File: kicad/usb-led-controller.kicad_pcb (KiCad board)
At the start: 4 copper layers, 70 x 30 mm, 99 parts, among them J1 SWD, J2 PWR, J3 USB, J4 PWM_0, J5 PWM_1, J6 WS2812_0, J7 WS2812_1, Q1 NVS4409N, Q2 NVS4409N, Q3 NVS4409N, Q4 NVS4409N, Q5 NVS4409N, Q6 NVS4409N, U1 SN74LV1T125, U2 SN74LV1T125, U3 EFM32HG308F64G-C-QFN24, U5 USBLC6

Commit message: Upgrading to Kicad 6
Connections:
- net /WS2812_0_~OE renamed /WS2812_0_~{OE}
- net /WS2812_1_~OE renamed /WS2812_1_~{OE}
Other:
- net class Default removed
- net class Power removed
- net class USB removed

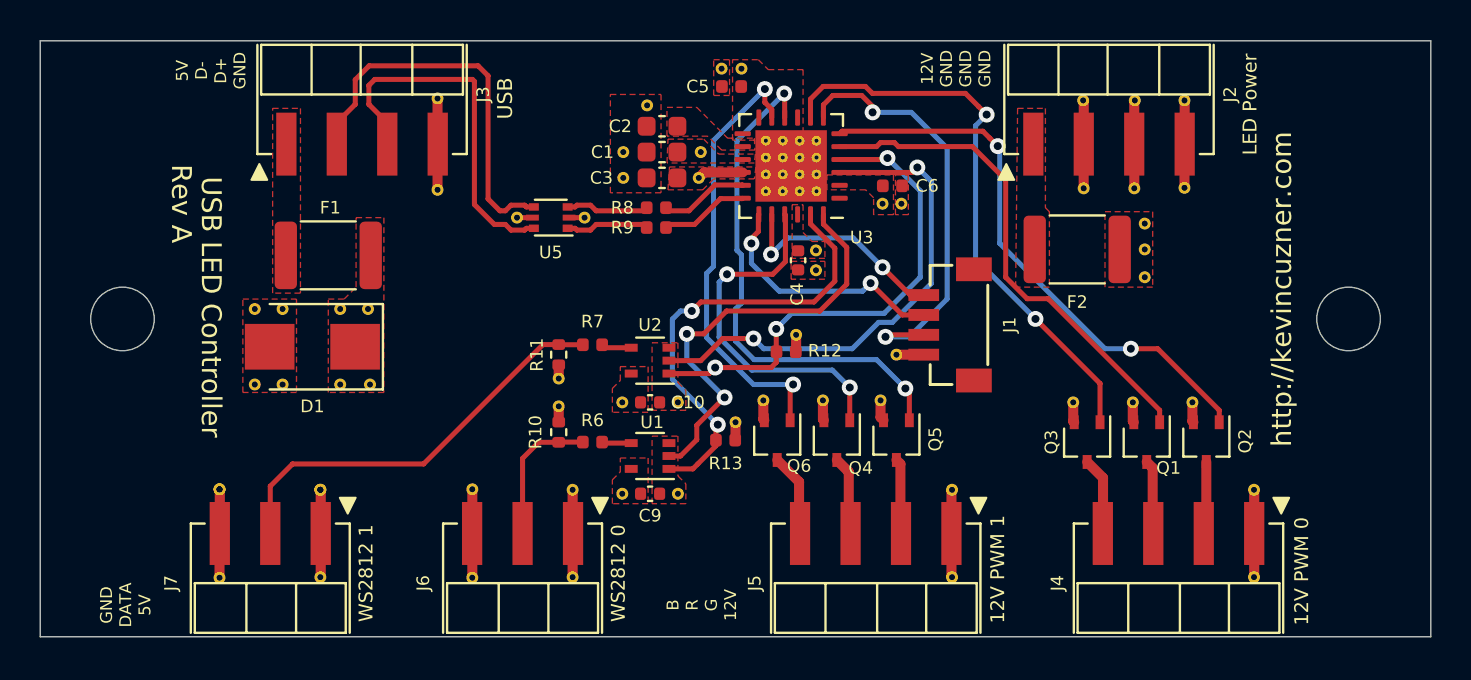
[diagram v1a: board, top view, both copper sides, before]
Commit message: Changing microcontroller to ATSAMD21E15B
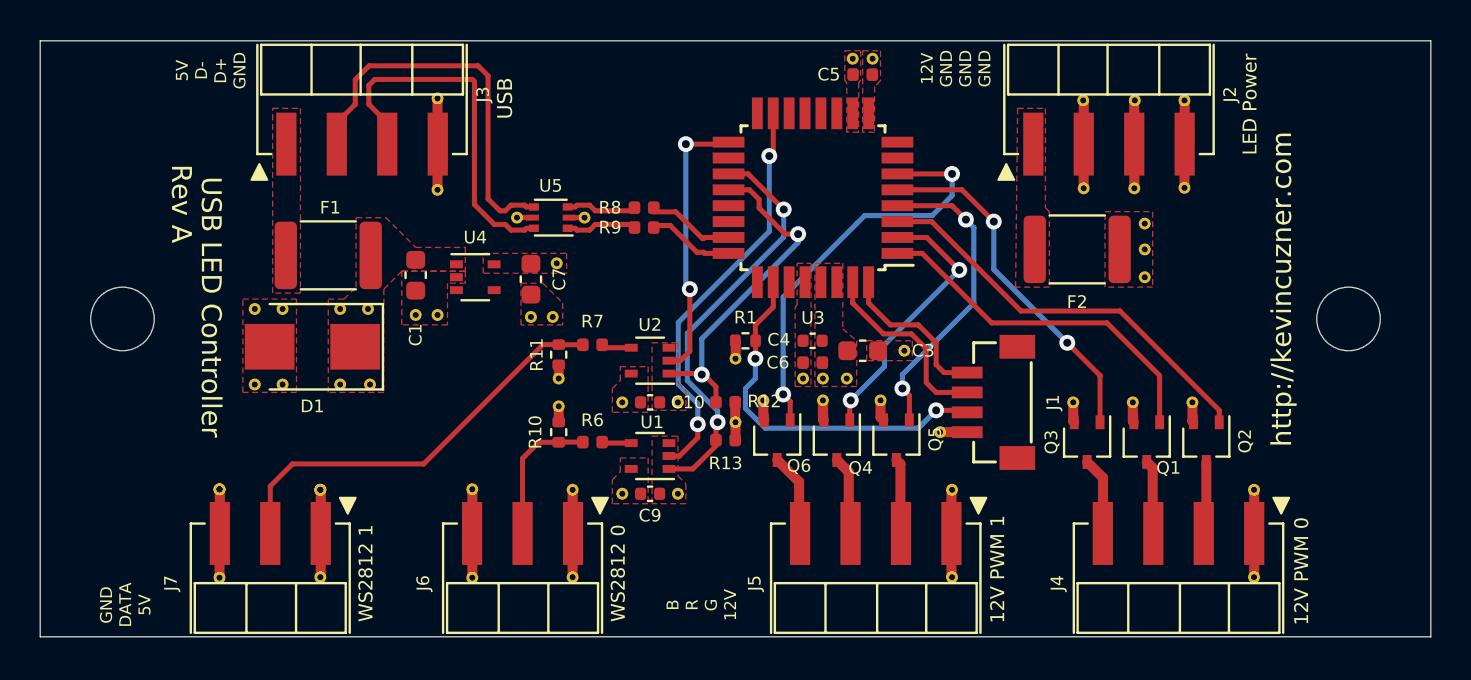
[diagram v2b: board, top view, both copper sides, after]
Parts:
- removed C2: 1u, Capacitor_SMD:C_0603_1608Metric
- removed the REF** at (163.2, 105.6)
- removed the REF** at (165.3, 101.4)
- added C7: 4u7, Capacitor_SMD:C_0603_1608Metric, F.Cu at (154.7, 112.0)
- added R1: 10K, Resistor_SMD:R_0402_1005Metric, F.Cu at (165.5, 115.1)
- added REF**: VIA-0.3_0.6-TENT, usb-led-controller:VIA-0.3_0.6-TENT, F.Cu at (175.3, 119.7)
- added REF**: VIA-0.3_0.6-TENT, usb-led-controller:VIA-0.3_0.6-TENT, F.Cu at (165.0, 116.0)
- added U4: MIC5365-3.3YC5, Package_TO_SOT_SMD:SOT-353_SC-70-5, F.Cu at (151.9, 111.9)
- U3: value EFM32HG308F64G-C-QFN24 -> ATSAMD21E15B-A; footprint Package_DFN_QFN:QFN-24-1EP_5x5mm_P0.65mm_EP3.6x3.6mm_ThermalVias -> Package_QFP:TQFP-32_7x7mm_P0.8mm
- moved REF** 18.5 mm to (155.8, 113.9)
- moved C1 13.9 mm to (148.9, 111.8), turned to -90 degrees
- moved C3 13.3 mm to (171.4, 115.6), turned to 0 degrees
- moved REF** 13.3 mm to (148.9, 113.8)
- moved REF** 12.2 mm to (154.7, 113.9)
- moved REF** 11.6 mm to (150.0, 113.8)
- moved C6 9.76 mm to (168.9, 116.2), turned to 180 degrees
- moved REF** 8.34 mm to (156.0, 111.2)
- moved REF** 7.32 mm to (171.9, 100.9)
- moved C5 6.63 mm to (171.4, 101.7)
- moved REF** 6.62 mm to (170.9, 100.9)
- moved REF** 6.46 mm to (169.4, 117.0)
- moved REF** 5.49 mm to (168.4, 117.0)
- moved J1 4.47 mm to (180.1, 118.2)
- moved C4 4.12 mm to (168.9, 115.1), turned to 180 degrees
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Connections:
- U3 pad 1: Net-(U3-Pad1) -> /GATE_0_R
- U3 pad 10: /GATE_1_G -> GND
- U3 pad 11: /GATE_1_B -> unconnected-(U3-Pad11)
- U3 pad 12: +3V3 -> unconnected-(U3-Pad12)
- U3 pad 13: +3V3 -> unconnected-(U3-Pad13)
- U3 pad 14: /UC_DECOUPLE -> unconnected-(U3-Pad14)
- U3 pad 15: +5V -> /WS2812_0_DATA_UC
- U3 pad 16: +3V3 -> unconnected-(U3-Pad16)
- U3 pad 17: /USB_D_R- -> /WS2812_1_DATA_UC
- U3 pad 18: /USB_D_R+ -> unconnected-(U3-Pad18)
- U3 pad 19: /SWCLK -> /WS2812_0_~{OE}
- U3 pad 2: +3V3 -> /GATE_1_R
- U3 pad 20: /SWDIO -> /WS2812_1_~{OE}
- U3 pad 21: /GATE_1_R -> unconnected-(U3-Pad21)
- U3 pad 22: +3V3 -> unconnected-(U3-Pad22)
- U3 pad 23: /WS2812_0_~{OE} -> /USB_D_R-
- U3 pad 24: /WS2812_0_DATA_UC -> /USB_D_R+
- U3 pad 25: GND -> unconnected-(U3-Pad25)
- U3 pad 3: /WS2812_1_DATA_UC -> /GATE_0_G
- U3 pad 4: /WS2812_1_~{OE} -> /GATE_1_G
- U3 pad 5: /GATE_0_R -> /GATE_0_B
- U3 pad 6: /GATE_0_G -> /GATE_1_B
- U3 pad 7: /NRST -> unconnected-(U3-Pad7)
- U3 pad 8: /GATE_0_B -> unconnected-(U3-Pad8)
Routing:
- net /WS2812_1_DATA_UC: track 25.4 -> 13.9 mm
- net /GATE_0_B: track 29.0 -> 17.8 mm
- net /GATE_1_G: track 26.1 -> 15.6 mm
- net /GATE_0_G: track 28.4 -> 20.7 mm, vias 2 -> 0
- net /WS2812_1_~{OE}: track 24.8 -> 17.3 mm, vias 3 -> 2
- net /GATE_0_R: track 25.3 -> 18.1 mm
- net /GATE_1_R: track 18.2 -> 13.6 mm
- net /SWDIO: track 11.3 -> 8.11 mm, vias 2 -> 0
- net /SWCLK: track 12.7 -> 9.67 mm, vias 2 -> 0
- net /NRST: track 21.8 -> 18.9 mm
- net /WS2812_0_~{OE}: track 23.0 -> 20.9 mm
- net /GATE_1_B: track 22.5 -> 20.8 mm
- net +3V3: track 4.08 -> 2.82 mm
- net GND: track 37.6 -> 36.6 mm
- net /WS2812_0_DATA_UC: track 21.5 -> 20.5 mm
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- removed copper zone on F.Cu, net /UC_DECOUPLE

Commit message: Changing programmer header to standard ARM Cortex one
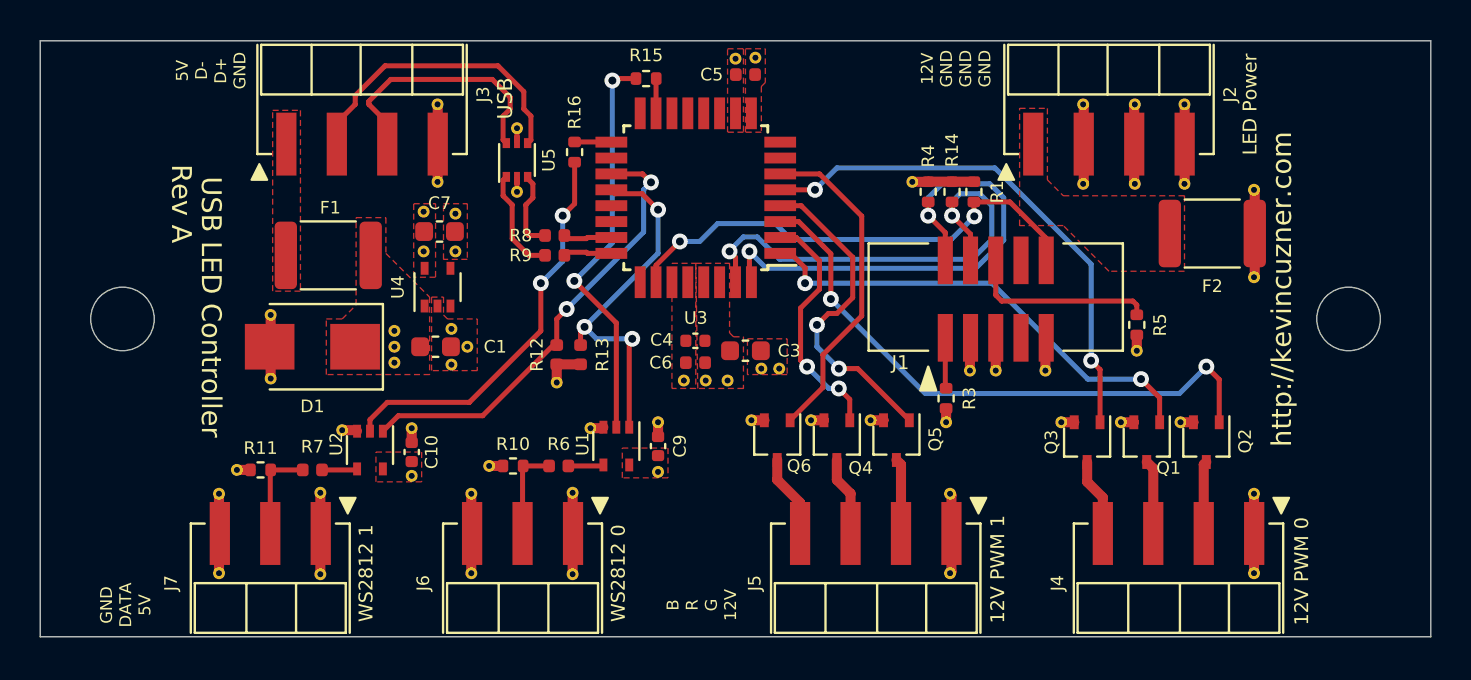
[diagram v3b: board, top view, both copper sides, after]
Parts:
- removed the REF** at (182.5, 107.4)
- removed the REF** at (150.0, 107.5)
- removed the REF** at (140.8, 117.3)
- removed the REF** at (142.2, 117.3)
- removed the REF** at (142.2, 113.5)
- removed the REF** at (140.8, 113.5)
- removed the REF** at (145.1, 117.3)
- removed the REF** at (146.6, 117.3)
- removed the REF** at (146.5, 113.5)
- removed the REF** at (145.1, 113.5)
- removed the REF** at (185.6, 111.9)
- removed the REF** at (185.1, 107.4)
- removed the REF** at (191.1, 122.6)
- removed the REF** at (182.0, 118.2)
- removed the REF** at (169.4, 118.1)
- removed the REF** at (166.4, 118.1)
- removed the REF** at (188.0, 118.2)
- removed the REF** at (175.9, 127.0)
- removed the REF** at (191.1, 127.0)
- removed the REF** at (185.0, 118.2)
- removed the REF** at (175.9, 122.6)
- removed the REF** at (172.3, 118.1)
- removed the REF** at (187.6, 107.4)
- removed the REF** at (156.8, 127.0)
- removed the REF** at (144.1, 122.6) (x2)
- removed the REF** at (139.0, 127.0)
- removed the REF** at (144.1, 127.0)
- removed the REF** at (139.0, 122.6) (x2)
- removed the REF** at (151.8, 127.0)
- removed the REF** at (151.8, 122.6)
- removed the REF** at (156.8, 122.6)
- removed the REF** at (187.6, 103.0)
- removed the REF** at (154.7, 113.9)
- removed the REF** at (148.9, 113.8)
- removed the REF** at (156.0, 111.2)
- removed the REF** at (169.4, 117.0)
- removed the REF** at (171.9, 100.9)
- removed the REF** at (159.3, 122.8)
- removed the REF** at (159.3, 118.2)
- removed the REF** at (154.0, 108.9)
- removed the REF** at (157.4, 108.9)
- removed the REF** at (170.9, 100.9)
- removed the REF** at (185.1, 103.0)
- removed the REF** at (155.8, 113.9)
- removed the REF** at (168.4, 117.0)
- removed the REF** at (162.1, 122.8)
- removed the REF** at (162.1, 118.2)
- removed the REF** at (156.1, 118.4)
- removed the REF** at (156.1, 117.0)
- removed the REF** at (173.5, 115.6)
- removed the REF** at (170.6, 117.0)
- removed the REF** at (165.0, 119.2)
- removed the REF** at (150.0, 113.8)
- removed the REF** at (182.5, 103.0)
- removed the REF** at (175.3, 119.7)
- removed the REF** at (165.0, 116.0)
- removed the REF** at (185.6, 110.5)
- removed the REF** at (185.6, 109.2)
- removed the REF** at (150.0, 102.9)
- added R14: 10K, Resistor_SMD:R_0402_1005Metric, F.Cu at (175.9, 107.6)
- added R15: 33, Resistor_SMD:R_0402_1005Metric, F.Cu at (160.5, 101.9)
- added R16: 33, Resistor_SMD:R_0402_1005Metric, F.Cu at (156.9, 105.6)
- added R3: 0, Resistor_SMD:R_0402_1005Metric, F.Cu at (175.6, 118.0)
- added R4: 10K, Resistor_SMD:R_0402_1005Metric, F.Cu at (174.7, 107.6)
- added R5: 10K, Resistor_SMD:R_0402_1005Metric, F.Cu at (185.2, 114.3)
- added REF**: VIA-0.3_0.6-TENT, usb-led-controller:VIA-0.3_0.6-TENT, F.Cu at (182.5, 107.2)
- added REF**: VIA-0.3_0.6-TENT, usb-led-controller:VIA-0.3_0.6-TENT, F.Cu at (165.0, 100.9)
- added REF**: VIA-0.3_0.6-TENT, usb-led-controller:VIA-0.3_0.6-TENT, F.Cu at (151.7, 122.8)
- added REF**: VIA-0.3_0.6-TENT, usb-led-controller:VIA-0.3_0.6-TENT, F.Cu at (161.1, 119.2)
- added REF**: VIA-0.3_0.6-TENT, usb-led-controller:VIA-0.3_0.6-TENT, F.Cu at (182.5, 103.2)
- added REF**: VIA-0.3_0.6-TENT, usb-led-controller:VIA-0.3_0.6-TENT, F.Cu at (168.8, 119.1)
- added REF**: VIA-0.3_0.6-TENT, usb-led-controller:VIA-0.3_0.6-TENT, F.Cu at (161.1, 121.7)
- added REF**: VIA-0.3_0.6-TENT, usb-led-controller:VIA-0.3_0.6-TENT, F.Cu at (151.5, 115.4)
- added REF**: VIA-0.3_0.6-TENT, usb-led-controller:VIA-0.3_0.6-TENT, F.Cu at (149.3, 110.6)
- added REF**: VIA-0.3_0.6-TENT, usb-led-controller:VIA-0.3_0.6-TENT, F.Cu at (176.8, 116.6)
- added REF**: VIA-0.3_0.6-TENT, usb-led-controller:VIA-0.3_0.6-TENT, F.Cu at (162.4, 117.1)
- added REF**: VIA-0.3_0.6-TENT, usb-led-controller:VIA-0.3_0.6-TENT, F.Cu at (145.2, 119.6)
- added REF**: VIA-0.3_0.6-TENT, usb-led-controller:VIA-0.3_0.6-TENT, F.Cu at (163.5, 117.1)
- added REF**: VIA-0.3_0.6-TENT, usb-led-controller:VIA-0.3_0.6-TENT, F.Cu at (165.8, 119.1)
- added REF**: VIA-0.3_0.6-TENT, usb-led-controller:VIA-0.3_0.6-TENT, F.Cu at (150.9, 110.6)
- added REF**: VIA-0.3_0.6-TENT, usb-led-controller:VIA-0.3_0.6-TENT, F.Cu at (144.1, 122.8)
- added REF**: VIA-0.3_0.6-TENT, usb-led-controller:VIA-0.3_0.6-TENT, F.Cu at (150.7, 116.3)
- added REF**: VIA-0.3_0.6-TENT, usb-led-controller:VIA-0.3_0.6-TENT, F.Cu at (181.4, 119.2)
- added REF**: VIA-0.3_0.6-TENT, usb-led-controller:VIA-0.3_0.6-TENT, F.Cu at (185.2, 115.6)
- added REF**: VIA-0.3_0.6-TENT, usb-led-controller:VIA-0.3_0.6-TENT, F.Cu at (173.9, 107.1)
- added REF**: VIA-0.3_0.6-TENT, usb-led-controller:VIA-0.3_0.6-TENT, F.Cu at (184.4, 119.2)
- added REF**: VIA-0.3_0.6-TENT, usb-led-controller:VIA-0.3_0.6-TENT, F.Cu at (187.6, 103.2)
- added REF**: VIA-0.3_0.6-TENT, usb-led-controller:VIA-0.3_0.6-TENT, F.Cu at (151.7, 126.8)
- added REF**: VIA-0.3_0.6-TENT, usb-led-controller:VIA-0.3_0.6-TENT, F.Cu at (147.8, 116.2)
- added REF**: VIA-0.3_0.6-TENT, usb-led-controller:VIA-0.3_0.6-TENT, F.Cu at (157.7, 119.5)
- added REF**: VIA-0.3_0.6-TENT, usb-led-controller:VIA-0.3_0.6-TENT, F.Cu at (156.0, 117.2)
- added REF**: VIA-0.3_0.6-TENT, usb-led-controller:VIA-0.3_0.6-TENT, F.Cu at (187.6, 107.2)
- added REF**: VIA-0.3_0.6-TENT, usb-led-controller:VIA-0.3_0.6-TENT, F.Cu at (185.1, 103.2)
- added REF**: VIA-0.3_0.6-TENT, usb-led-controller:VIA-0.3_0.6-TENT, F.Cu at (156.8, 122.8)
- added REF**: VIA-0.3_0.6-TENT, usb-led-controller:VIA-0.3_0.6-TENT, F.Cu at (175.8, 126.8)
- added REF**: VIA-0.3_0.6-TENT, usb-led-controller:VIA-0.3_0.6-TENT, F.Cu at (150.0, 107.1)
- added REF**: VIA-0.3_0.6-TENT, usb-led-controller:VIA-0.3_0.6-TENT, F.Cu at (139.9, 121.6)
- added REF**: VIA-0.3_0.6-TENT, usb-led-controller:VIA-0.3_0.6-TENT, F.Cu at (191.1, 126.8)
- added REF**: VIA-0.3_0.6-TENT, usb-led-controller:VIA-0.3_0.6-TENT, F.Cu at (147.8, 114.6)
- added REF**: VIA-0.3_0.6-TENT, usb-led-controller:VIA-0.3_0.6-TENT, F.Cu at (178.1, 116.6)
- added REF**: VIA-0.3_0.6-TENT, usb-led-controller:VIA-0.3_0.6-TENT, F.Cu at (154.0, 107.6)
- added REF**: VIA-0.3_0.6-TENT, usb-led-controller:VIA-0.3_0.6-TENT, F.Cu at (166.0, 100.8)
- added REF**: VIA-0.3_0.6-TENT, usb-led-controller:VIA-0.3_0.6-TENT, F.Cu at (166.3, 116.5)
- added REF**: VIA-0.3_0.6-TENT, usb-led-controller:VIA-0.3_0.6-TENT, F.Cu at (175.8, 122.8)
- added REF**: VIA-0.3_0.6-TENT, usb-led-controller:VIA-0.3_0.6-TENT, F.Cu at (191.1, 111.9)
- added REF**: VIA-0.3_0.6-TENT, usb-led-controller:VIA-0.3_0.6-TENT, F.Cu at (144.1, 126.8)
- added REF**: VIA-0.3_0.6-TENT, usb-led-controller:VIA-0.3_0.6-TENT, F.Cu at (171.8, 119.1)
- added REF**: VIA-0.3_0.6-TENT, usb-led-controller:VIA-0.3_0.6-TENT, F.Cu at (141.6, 113.8)
- added REF**: VIA-0.3_0.6-TENT, usb-led-controller:VIA-0.3_0.6-TENT, F.Cu at (191.1, 122.8)
- added REF**: VIA-0.3_0.6-TENT, usb-led-controller:VIA-0.3_0.6-TENT, F.Cu at (164.6, 117.1)
- added REF**: VIA-0.3_0.6-TENT, usb-led-controller:VIA-0.3_0.6-TENT, F.Cu at (154.0, 104.4)
- added REF**: VIA-0.3_0.6-TENT, usb-led-controller:VIA-0.3_0.6-TENT, F.Cu at (141.6, 117.0)
- added REF**: VIA-0.3_0.6-TENT, usb-led-controller:VIA-0.3_0.6-TENT, F.Cu at (148.7, 119.5)
- added REF**: VIA-0.3_0.6-TENT, usb-led-controller:VIA-0.3_0.6-TENT, F.Cu at (175.6, 119.2)
- added REF**: VIA-0.3_0.6-TENT, usb-led-controller:VIA-0.3_0.6-TENT, F.Cu at (167.2, 116.5)
- added REF**: VIA-0.3_0.6-TENT, usb-led-controller:VIA-0.3_0.6-TENT, F.Cu at (150.7, 114.5)
- added REF**: VIA-0.3_0.6-TENT, usb-led-controller:VIA-0.3_0.6-TENT, F.Cu at (180.6, 116.6)
- added REF**: VIA-0.3_0.6-TENT, usb-led-controller:VIA-0.3_0.6-TENT, F.Cu at (185.1, 107.2)
- added REF**: VIA-0.3_0.6-TENT, usb-led-controller:VIA-0.3_0.6-TENT, F.Cu at (149.3, 108.6)
- added REF**: VIA-0.3_0.6-TENT, usb-led-controller:VIA-0.3_0.6-TENT, F.Cu at (187.4, 119.2)
- added REF**: VIA-0.3_0.6-TENT, usb-led-controller:VIA-0.3_0.6-TENT, F.Cu at (150.0, 103.2)
- added REF**: VIA-0.3_0.6-TENT, usb-led-controller:VIA-0.3_0.6-TENT, F.Cu at (150.9, 108.7)
- added REF**: VIA-0.3_0.6-TENT, usb-led-controller:VIA-0.3_0.6-TENT, F.Cu at (147.8, 115.4)
- added REF**: VIA-0.3_0.6-TENT, usb-led-controller:VIA-0.3_0.6-TENT, F.Cu at (139.0, 126.8)
- added REF**: VIA-0.3_0.6-TENT, usb-led-controller:VIA-0.3_0.6-TENT, F.Cu at (191.1, 107.5)
- added REF**: VIA-0.3_0.6-TENT, usb-led-controller:VIA-0.3_0.6-TENT, F.Cu at (148.7, 121.9)
- added REF**: VIA-0.3_0.6-TENT, usb-led-controller:VIA-0.3_0.6-TENT, F.Cu at (139.0, 122.8)
- added REF**: VIA-0.3_0.6-TENT, usb-led-controller:VIA-0.3_0.6-TENT, F.Cu at (156.8, 126.8)
- added REF**: VIA-0.3_0.6-TENT, usb-led-controller:VIA-0.3_0.6-TENT, F.Cu at (152.6, 121.4)
- J1: value SWD -> CORTEX-M JTAG; footprint usb-led-controller:JST-SH-4 -> usb-led-controller:CORTEX-SWD-CONNECTOR
- moved R11 16.1 mm to (141.1, 121.6), turned to 180 degrees
- moved R7 15.4 mm to (143.7, 121.6)
- moved U2 14.8 mm to (146.6, 120.6), turned to -90 degrees
- moved R1 13.7 mm to (177.0, 107.6), turned to -90 degrees
- moved C10 12.3 mm to (148.7, 120.7), turned to 90 degrees
- moved R12 8.83 mm to (156.0, 115.8), turned to 90 degrees
- moved R13 8.47 mm to (157.2, 115.8), turned to 90 degrees
- moved F2 6.85 mm to (189.0, 109.7)
- moved C3 5.90 mm to (165.5, 115.6)
- moved C4 5.90 mm to (163.0, 115.1)
- moved C5 5.90 mm to (165.5, 101.7)
- moved U3 5.90 mm to (163.0, 107.9)
- moved C6 5.90 mm to (163.0, 116.2)
- moved J1 5.57 mm to (178.1, 113.0), turned to 0 degrees
- moved C7 5.19 mm to (150.1, 109.6), turned to 0 degrees
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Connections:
- J1 pad 1: GND -> /3V3_JTAG
- J1 pad 2: /NRST -> /SWDIO
- J1 pad 3: /SWCLK -> GND
- J1 pad 4: /SWDIO -> /SWCLK
- U3 pad 15: /WS2812_0_DATA_UC -> /WS2812_1_DATA_UC_R
- U3 pad 17: /WS2812_1_DATA_UC -> /WS2812_0_DATA_UC_R
- U3 pad 19: /WS2812_0_~{OE} -> /WS2812_1_~{OE}
- U3 pad 20: /WS2812_1_~{OE} -> /WS2812_0_~{OE}
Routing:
- net /SWDIO: track 8.11 -> 26.0 mm, vias 0 -> 2
- net /WS2812_1_DATA: track 21.1 -> 4.82 mm
- net /SWCLK: track 9.67 -> 24.2 mm, vias 0 -> 2
- net /SWO: track 0.00 -> 9.55 mm
- net /GATE_0_G: track 20.7 -> 30.0 mm, vias 0 -> 2
- net /GATE_0_B: track 17.8 -> 26.3 mm
- net /WS2812_1_DATA_UC: track 13.9 -> 20.2 mm
- net /NRST: track 18.9 -> 24.8 mm
- net /GATE_0_R: track 18.1 -> 23.8 mm, vias 0 -> 2
- net /WS2812_1_~{OE}: track 17.3 -> 22.9 mm
- net /USB_D+: track 18.6 -> 13.0 mm
- net GND: track 36.6 -> 41.9 mm
- net /USB_D-: track 19.7 -> 15.3 mm
- net /GATE_1_B: track 20.8 -> 16.8 mm, vias 2 -> 0
- net +12V: track 8.83 -> 12.5 mm
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- removed copper zone on F.Cu, net +12V

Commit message: Changing FET selection, fixing stackup, adding CYA resistors
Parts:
- added R17: 33, Resistor_SMD:R_0402_1005Metric, F.Cu at (163.2, 101.9)
- added R18: 33, Resistor_SMD:R_0402_1005Metric, F.Cu at (166.3, 114.0)
- added R2: 10K, Resistor_SMD:R_0402_1005Metric, F.Cu at (152.2, 112.9)
- added REF**: VIA-0.3_0.6-TENT, usb-led-controller:VIA-0.3_0.6-TENT, F.Cu at (152.8, 114.0)
- added TP1: SWO, TestPoint:TestPoint_Pad_D1.5mm, F.Cu at (189.1, 114.1)
- Q1, Q2, Q3, Q4, Q5, Q6: value NVS4409N -> Si1078X; footprint Package_TO_SOT_SMD:SOT-323_SC-70 -> usb-led-controller:SC-89
- moved REF** 2.62 mm to (169.6, 121.6)
- moved REF** 2.62 mm to (166.6, 121.6)
- moved REF** 2.62 mm to (172.6, 121.6)
- moved REF** 2.55 mm to (184.9, 121.7)
- moved REF** 2.53 mm to (181.8, 121.7)
- moved REF** 2.53 mm to (187.8, 121.7)
- moved R5 0.90 mm to (186.1, 114.3)
- moved REF** 0.90 mm to (186.1, 115.6)
- moved Q2 0.30 mm to (188.4, 120.2)
- moved Q3 0.30 mm to (182.4, 120.2)
- moved Q1 0.20 mm to (185.5, 120.2)
- moved Q4 0.10 mm to (170.2, 120.1)
- moved Q5 0.10 mm to (173.2, 120.1)
- moved Q6 0.10 mm to (167.2, 120.1)
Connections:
- Q1 pad 1: /GATE_0_R -> /PWM_0_R
- Q1 pad 2: GND -> /GATE_0_R
- Q1 pad 3: /PWM_0_R -> GND
- Q2 pad 1: /GATE_0_G -> /PWM_0_G
- Q2 pad 2: GND -> /GATE_0_G
- Q2 pad 3: /PWM_0_G -> GND
- Q3 pad 1: /GATE_0_B -> /PWM_0_B
- Q3 pad 2: GND -> /GATE_0_B
- Q3 pad 3: /PWM_0_B -> GND
- Q4 pad 1: /GATE_1_R -> /PWM_1_R
- Q4 pad 2: GND -> /GATE_1_R
- Q4 pad 3: /PWM_1_R -> GND
- Q5 pad 1: /GATE_1_G -> /PWM_1_G
- Q5 pad 2: GND -> /GATE_1_G
- Q5 pad 3: /PWM_1_G -> GND
- Q6 pad 1: /GATE_1_B -> /PWM_1_B
- Q6 pad 2: GND -> /GATE_1_B
- Q6 pad 3: /PWM_1_B -> GND
- U3 pad 11: unconnected-(U3-Pad11) -> /SWO_UC
- U3 pad 3: /GATE_0_G -> unconnected-(U3-Pad3)
- U3 pad 32: /SWDIO -> /SWDIO_UC
- U3 pad 4: /GATE_1_G -> unconnected-(U3-Pad4)
- U3 pad 5: /GATE_0_B -> /GATE_0_G
- U3 pad 6: /GATE_1_B -> /GATE_1_G
- U3 pad 7: unconnected-(U3-Pad7) -> /GATE_0_B
- U3 pad 8: unconnected-(U3-Pad8) -> /GATE_1_B
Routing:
- net /SWO: track 9.55 -> 43.8 mm, vias 0 -> 2
- net GND: track 41.9 -> 37.3 mm
- net /PWM_1_B: track 4.18 -> 0.00 mm
- net /GATE_0_G: track 30.0 -> 34.0 mm
- net /PWM_1_R: track 3.99 -> 0.00 mm
- net /GATE_1_B: track 16.8 -> 20.7 mm, vias 0 -> 2
- net /PWM_0_B: track 3.93 -> 0.00 mm
- net /PWM_1_G: track 3.80 -> 0.00 mm
- net /PWM_0_R: track 3.74 -> 0.00 mm
- net /PWM_0_G: track 3.65 -> 0.00 mm
- net /3V3_EN: track 0.00 -> 2.30 mm
- net /SWO_UC: track 0.00 -> 1.95 mm
- net /SWDIO_UC: track 0.00 -> 1.90 mm
- net /USB_D+: track 13.0 -> 14.4 mm
- net /GATE_0_B: track 26.3 -> 27.6 mm
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- added copper zone on F.Cu, net /PWM_0_B
- added copper zone on F.Cu, net /PWM_0_G
- added copper zone on F.Cu, net /PWM_0_R
- added copper zone on F.Cu, net /PWM_1_B
- added copper zone on F.Cu, net /PWM_1_G
- added copper zone on F.Cu, net /PWM_1_R
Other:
- board text added: "Use stackup JLC3313"
